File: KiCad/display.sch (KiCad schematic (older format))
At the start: 72 parts, among them IC11 SN74LV1T125DBVR, IC6 PCA9517ADP, J1 46756-1001, J2 2129320-3, T1 BSS138APW

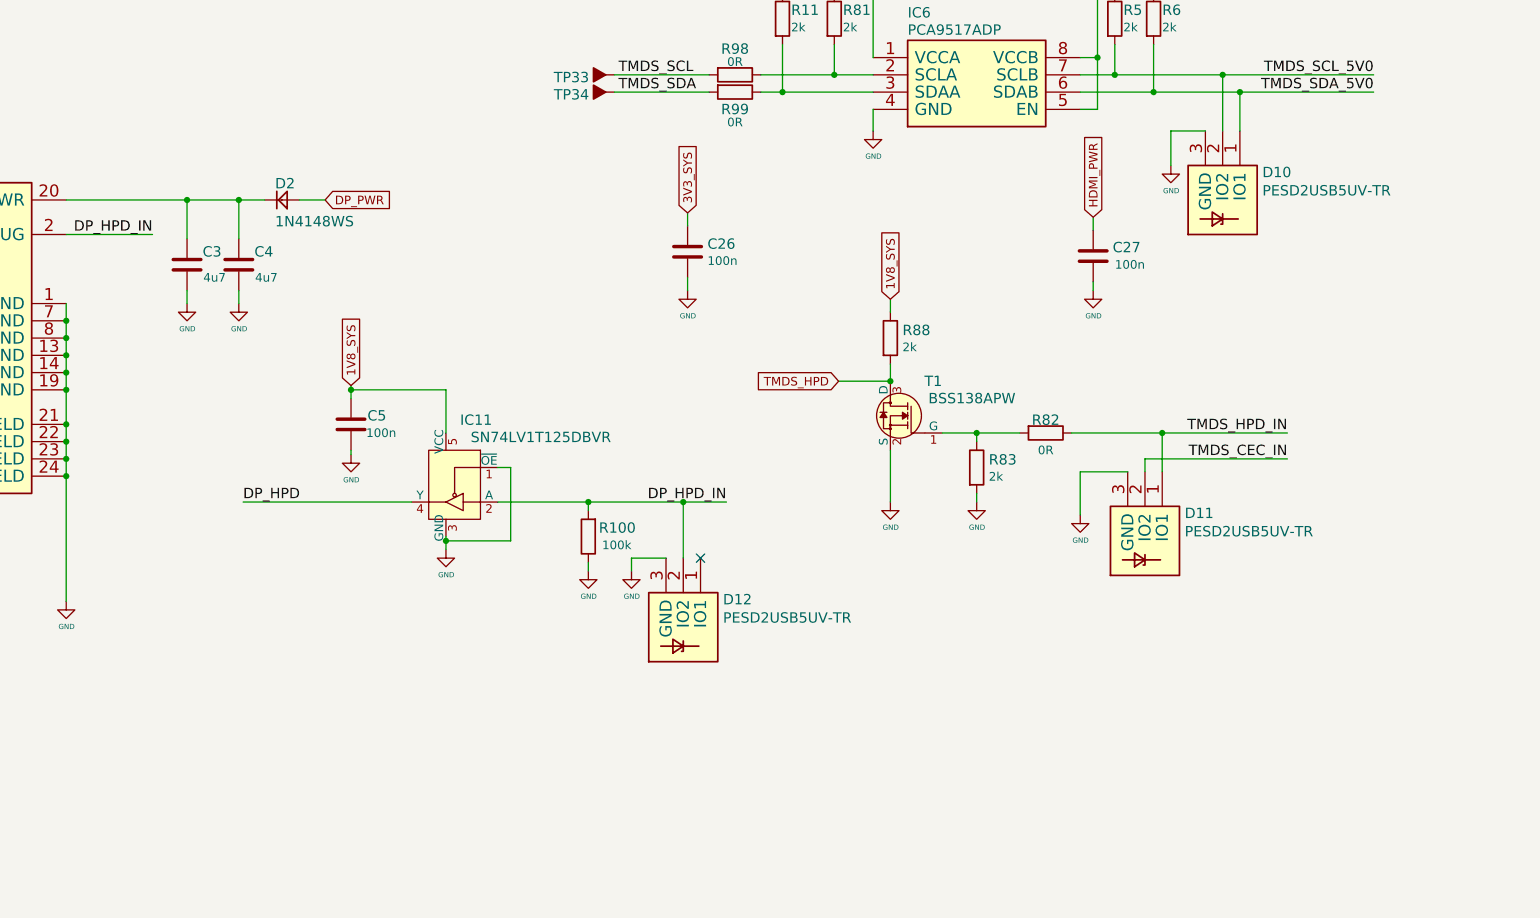
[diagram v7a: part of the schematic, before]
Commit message: Change PESD2USB5UV-TR and TPD4E05U06_PASS  to TPD4E05U06QDQARQ1
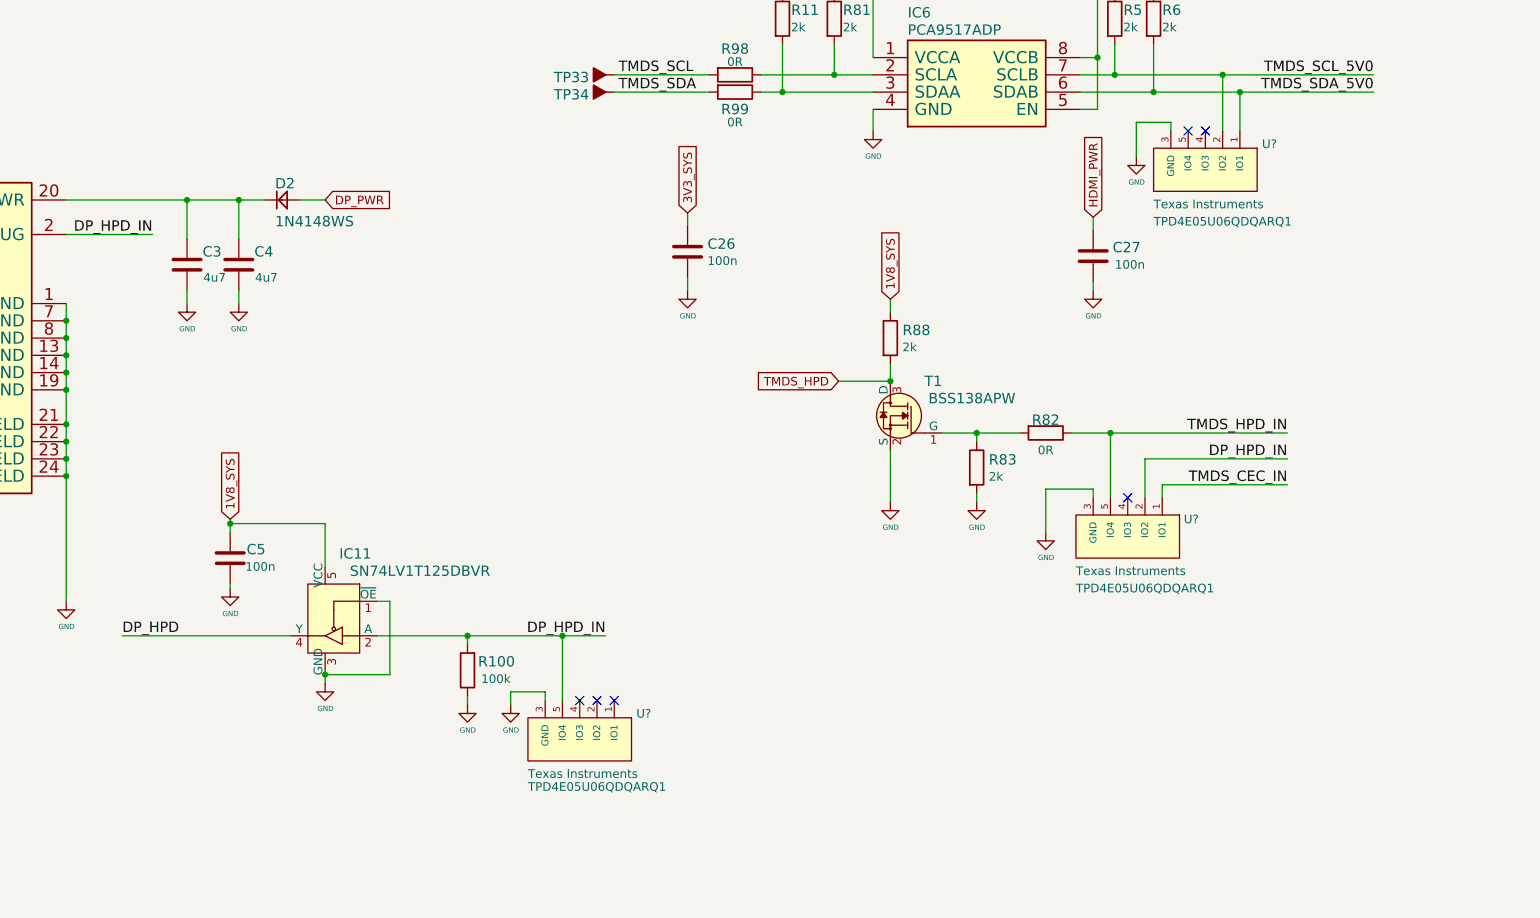
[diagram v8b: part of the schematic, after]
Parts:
- removed D10, D11, D12: PESD2USB5UV-TR, jetson-nano-baseboard-footprints:SOT-23s, symbol jetson-nano-baseboard:PESD2USB5UV-TR
- added U? (x3): TPD4E05U06QDQARQ1, jetson-nano-baseboard-footprints:TPD4E05U06QDQARQ1, symbol jetson-nano-baseboard:TPD4E05U06QDQARQ1
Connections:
- net DP_HPD_IN: now also U?.2 (IO2), U?.5 (IO4), U?.6 (IO4), U?.9 (IO2)
- net GND: now also U?.3 (GND), U?.3 (GND), U?.3 (GND), U?.8 (GND), U?.8 (GND), U?.8 (GND)
- net TMDS_CEC_IN: now also U?.1 (IO1), U?.10 (IO1)
- net TMDS_HPD_IN: now also U?.5 (IO4), U?.6 (IO4)
- net TMDS_SCL_5V0: now also U?.2 (IO2), U?.9 (IO2)
- net TMDS_SDA_5V0: now also U?.1 (IO1), U?.10 (IO1)
- new net: U?.4 (IO3), U?.7 (IO3) (x3)
- new net: U?.5 (IO4), U?.6 (IO4)
- new net: U?.1 (IO1), U?.10 (IO1)
- new net: U?.2 (IO2), U?.9 (IO2)
- no-connect marks 3 -> 8
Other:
- moved on the sheet: C5, IC11, R100
